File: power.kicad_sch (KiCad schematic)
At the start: 44 parts, among them IC1 MP9943AGQ-Z, IC2 MP9943AGQ-Z, U4 AP2112K-3.3TRG1, U5 AP2112K-1.8TRG1

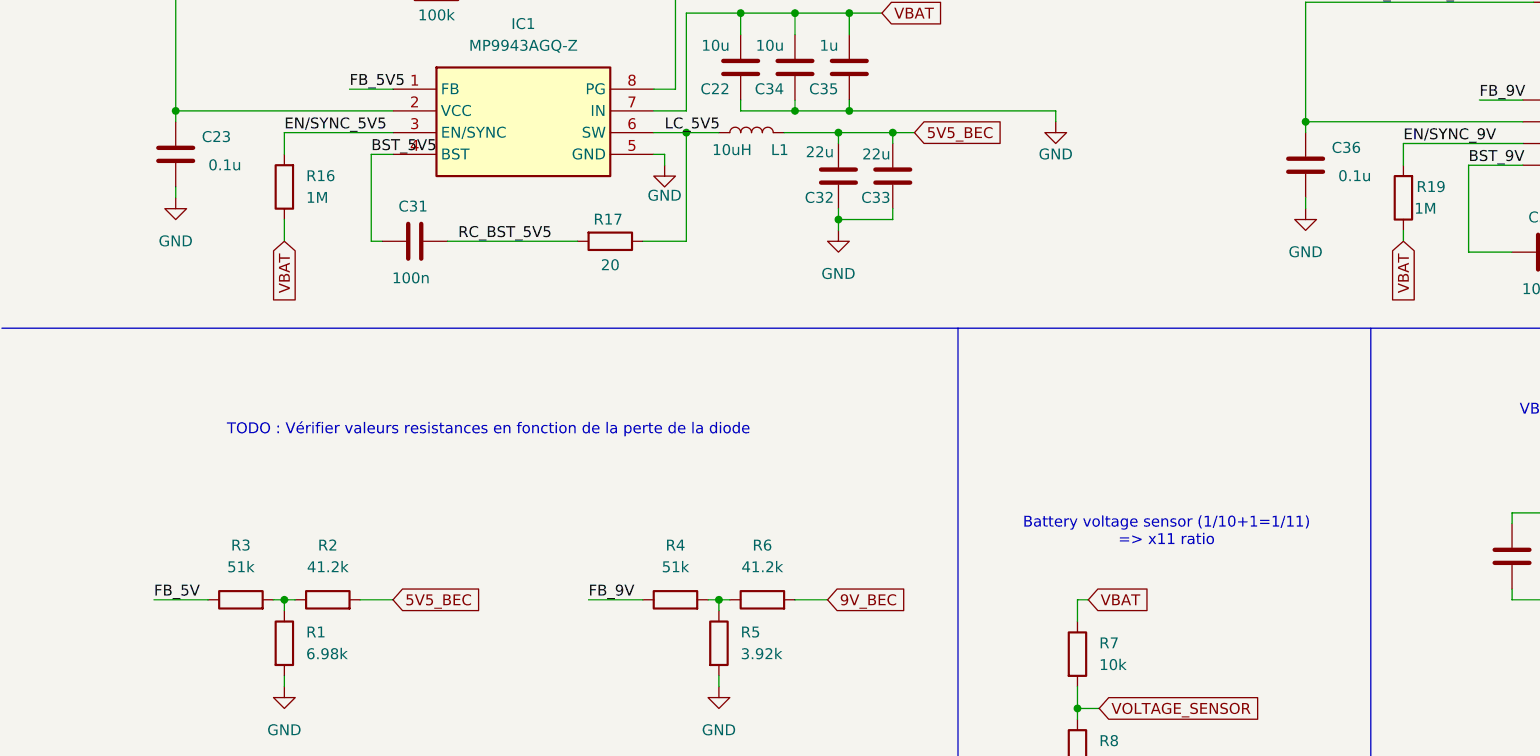
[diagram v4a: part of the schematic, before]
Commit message: - affected footprints for components - started placing components
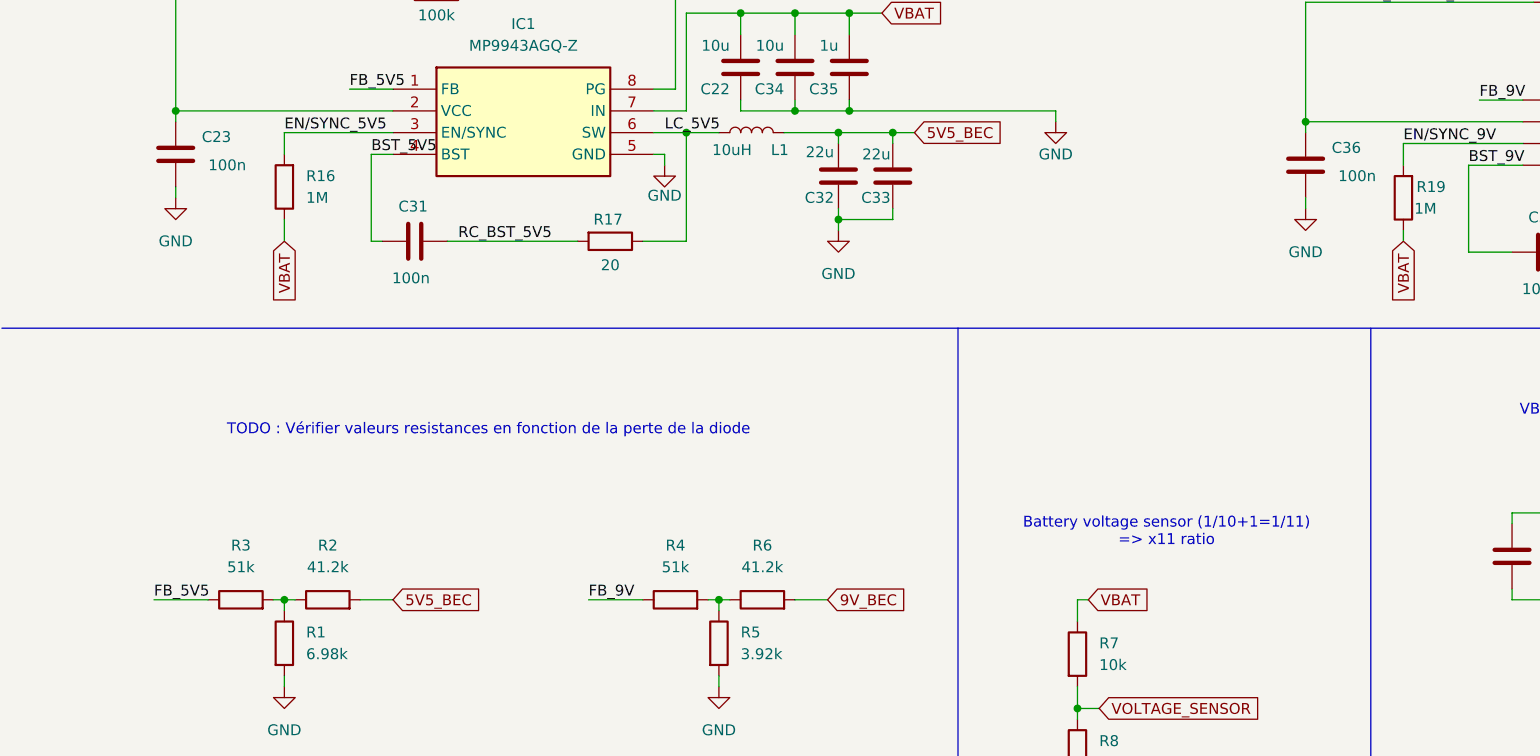
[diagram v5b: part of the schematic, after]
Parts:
- C1, C2, C20, C21, C22, C31, C34, C35, C37, C38, C39, C41: footprint (none) -> Capacitor_SMD:C_0402_1005Metric
- C16, C17, C18, C19, C32, C33, C40, C42: footprint (none) -> Capacitor_SMD:C_0603_1608Metric
- C23, C36: value 0.1u -> 100n; footprint (none) -> Capacitor_SMD:C_0402_1005Metric
- D1, D2: footprint SOD3716X145M -> fcg4_fp:SOD3716X145M
- IC1, IC2: footprint SON65P300X300X100-8M -> fcg4_fp:SON65P300X300X100-8M
- L1, L2: footprint (none) -> Inductor_SMD:L_0603_1608Metric; Manufacturer_Part_Number (none) -> LQM18DH100M70L
- R1, R16, R17, R18, R19, R2, R20, R21, R3, R4, R5, R6, R7, R8: footprint (none) -> Resistor_SMD:R_0402_1005Metric
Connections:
- net FB_5V is gone; now on net FB_5V5: R3.1
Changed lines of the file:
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@@
 		)
 	)
-	(label "FB_5V"
+	(label "FB_5V5"
 		(at 30.48 148.59 0)
 		(effects
@@
 			)
 		)
-		(property "Footprint" ""
+		(property "Footprint" "Capacitor_SMD:C_0402_1005Metric"
 			(at 108.9152 43.18 0)
 			(effects
@@
 			)
 		)
-		(property "Footprint" ""
+		(property "Footprint" "Capacitor_SMD:C_0603_1608Metric"
 			(at 241.6048 96.52 0)
 			(effects
@@
 			)
 		)
-		(property "Footprint" ""
+		(property "Footprint" "Resistor_SMD:R_0402_1005Metric"
 			(at 43.942 153.67 90)
 			(effects
@@
 			)
 		)
-		(property "Footprint" ""
+		(property "Footprint" "Capacitor_SMD:C_0402_1005Metric"
 			(at 104.4448 82.55 0)
 			(effects
@@
 			)
 		)
-		(property "Footprint" ""
+		(property "Footprint" "Capacitor_SMD:C_0603_1608Metric"
 			(at 201.6252 147.32 0)
 			(effects
@@
 			)
 		)
-		(property "Footprint" ""
+		(property "Footprint" "Resistor_SMD:R_0402_1005Metric"
 			(at 94.742 153.67 90)
 			(effects
@@
 			)
 		)
-		(property "Footprint" ""
+		(property "Footprint" "Capacitor_SMD:C_0603_1608Metric"
 			(at 190.1952 147.32 0)
 			(effects
@@
 			)
 		)
-		(property "Footprint" ""
+		(property "Footprint" "Resistor_SMD:R_0402_1005Metric"
 			(at 101.6 150.368 90)
 			(effects
@@
 			)
 		)
-		(property "Footprint" ""
+		(property "Footprint" "Capacitor_SMD:C_0603_1608Metric"
 			(at 247.9548 96.52 0)
 			(effects
@@
 			)
 		)
-		(property "Footprint" ""
+		(property "Footprint" "Capacitor_SMD:C_0603_1608Metric"
 			(at 224.4852 147.32 0)
 			(effects
@@
 			)
 		)
-		(property "Footprint" ""
+		(property "Footprint" "Capacitor_SMD:C_0402_1005Metric"
 			(at 110.7948 82.55 0)
 			(effects
@@
 			)
 		)
-		(property "Footprint" ""
+		(property "Footprint" "Capacitor_SMD:C_0402_1005Metric"
 			(at 98.0948 82.55 0)
 			(effects
@@
 			)
 		)
-		(property "Footprint" ""
+		(property "Footprint" "Resistor_SMD:R_0402_1005Metric"
 			(at 40.64 150.368 90)
 			(effects
@@
 			)
 		)
-		(property "Footprint" ""
+		(property "Footprint" "Capacitor_SMD:C_0603_1608Metric"
 			(at 115.8748 95.25 0)
 			(effects
@@
 			)
 		)
-		(property "Footprint" ""
+		(property "Footprint" "Capacitor_SMD:C_0402_1005Metric"
 			(at 64.77 105.7148 0)
 			(effects
@@
 			)
 		)
-		(property "Footprint" ""
+		(property "Footprint" "Capacitor_SMD:C_0603_1608Metric"
 			(at 213.0552 147.32 0)
 			(effects
@@
 			)
 		)
-		(property "Footprint" ""
+		(property "Footprint" "Capacitor_SMD:C_0402_1005Metric"
 			(at 196.85 106.9848 0)
 			(effects
@@
 			)
 		)
-		(property "Footprint" ""
+		(property "Footprint" "Resistor_SMD:R_0402_1005Metric"
 			(at 47.498 100.33 90)
 			(effects
@@
 			)
 		)
-		(property "Footprint" ""
+		(property "Footprint" "Resistor_SMD:R_0402_1005Metric"
 			(at 50.8 150.368 90)
 			(effects
@@
 			)
 		)
-		(property "Footprint" "SOD3716X145M"
+		(property "Footprint" "fcg4_fp:SOD3716X145M"
 			(at 58.42 -63.17 0)
 			(effects
@@
 			)
 		)
-		(property "Footprint" ""
+		(property "Footprint" "Capacitor_SMD:C_0402_1005Metric"
 			(at 242.8748 83.82 0)
 			(effects
@@
 			)
 		)
-		(property "Footprint" ""
+		(property "Footprint" "Capacitor_SMD:C_0402_1005Metric"
 			(at 230.1748 83.82 0)
 			(effects
@@
 			)
 		)
-		(property "Footprint" "SOD3716X145M"
+		(property "Footprint" "fcg4_fp:SOD3716X145M"
 			(at 41.91 -59.36 0)
 			(effects
@@
 			)
 		)
-		(property "Value" "0.1u"
+		(property "Value" "100n"
 			(at 168.91 99.0599 0)
 			(effects
@@
 			)
 		)
-		(property "Footprint" ""
+		(property "Footprint" "Capacitor_SMD:C_0402_1005Metric"
 			(at 166.0652 101.6 0)
 			(effects
@@
 			)
 		)
-		(property "Footprint" ""
+		(property "Footprint" "Resistor_SMD:R_0402_1005Metric"
 			(at 178.308 101.6 90)
 			(effects
@@
 			)
 		)
-		(property "Footprint" ""
+		(property "Footprint" "Inductor_SMD:L_0603_1608Metric"
 			(at 232.41 95.25 0)
 			(effects
@@
 			)
 		)
+		(property "Manufacturer_Part_Number" "LQM18DH100M70L"
+			(at 232.41 95.25 90)
+			(effects
+				(font
+					(size 1.27 1.27)
+				)
+				(hide yes)
+			)
+		)
 		(pin "1"
 		)
@@
 			)
 		)
-		(property "Footprint" ""
+		(property "Footprint" "Capacitor_SMD:C_0402_1005Metric"
 			(at 196.5452 44.45 0)
 			(effects
@@
 			)
 		)
-		(property "Footprint" ""
+		(property "Footprint" "Resistor_SMD:R_0402_1005Metric"
 			(at 215.9 106.172 90)
 			(effects
@@
 			)
 		)
-		(property "Footprint" ""
+		(property "Footprint" "Resistor_SMD:R_0402_1005Metric"
 			(at 136.652 154.94 90)
 			(effects
@@
 			)
 		)
-		(property "Footprint" ""
+		(property "Footprint" "Capacitor_SMD:C_0402_1005Metric"
 			(at 236.5248 83.82 0)
 			(effects
@@
 			)
 		)
-		(property "Footprint" "SON65P300X300X100-8M"
+		(property "Footprint" "fcg4_fp:SON65P300X300X100-8M"
 			(at 217.17 185.09 0)
 			(effects
@@
 			)
 		)
-		(property "Footprint" ""
+		(property "Footprint" "Resistor_SMD:R_0402_1005Metric"
 			(at 136.652 166.37 90)
 			(effects
@@
 			)
 		)
-		(property "Footprint" ""
+		(property "Footprint" "Resistor_SMD:R_0402_1005Metric"
 			(at 63.5 75.692 90)
 			(effects
@@
 			)
 		)
-		(property "Footprint" ""
+		(property "Footprint" "Inductor_SMD:L_0603_1608Metric"
 			(at 100.33 93.98 0)
 			(effects
@@
 			)
 		)
+		(property "Manufacturer_Part_Number" "LQM18DH100M70L"
+			(at 100.33 93.98 90)
+			(effects
+				(font
+					(size 1.27 1.27)
+				)
+				(hide yes)
+			)
+		)
 		(pin "1"
 		)
@@
 			)
 		)
-		(property "Value" "0.1u"
+		(property "Value" "100n"
 			(at 36.83 97.7899 0)
 			(effects
@@
 			)
 		)
-		(property "Footprint" ""
+		(property "Footprint" "Capacitor_SMD:C_0402_1005Metric"
 			(at 33.9852 100.33 0)
 			(effects
@@
 			)
 		)
-		(property "Footprint" ""
+		(property "Footprint" "Resistor_SMD:R_0402_1005Metric"
 			(at 83.82 104.902 90)
 			(effects
@@
 			)
 		)
-		(property "Footprint" ""
+		(property "Footprint" "Capacitor_SMD:C_0402_1005Metric"
 			(at 73.3552 46.99 0)
 			(effects
@@
 			)
 		)
-		(property "Footprint" ""
+		(property "Footprint" "Resistor_SMD:R_0402_1005Metric"
 			(at 195.58 76.962 90)
 			(effects
@@
 			)
 		)
-		(property "Footprint" ""
+		(property "Footprint" "Capacitor_SMD:C_0603_1608Metric"
 			(at 109.5248 95.25 0)
 			(effects
@@
 			)
 		)
-		(property "Footprint" ""
+		(property "Footprint" "Capacitor_SMD:C_0402_1005Metric"
 			(at 239.7252 44.45 0)
 			(effects
@@
 			)
 		)
-		(property "Footprint" ""
+		(property "Footprint" "Resistor_SMD:R_0402_1005Metric"
 			(at 91.44 150.368 90)
 			(effects
@@
 			)
 		)
-		(property "Footprint" "SON65P300X300X100-8M"
+		(property "Footprint" "fcg4_fp:SON65P300X300X100-8M"
 			(at 85.09 183.82 0)
 			(effects

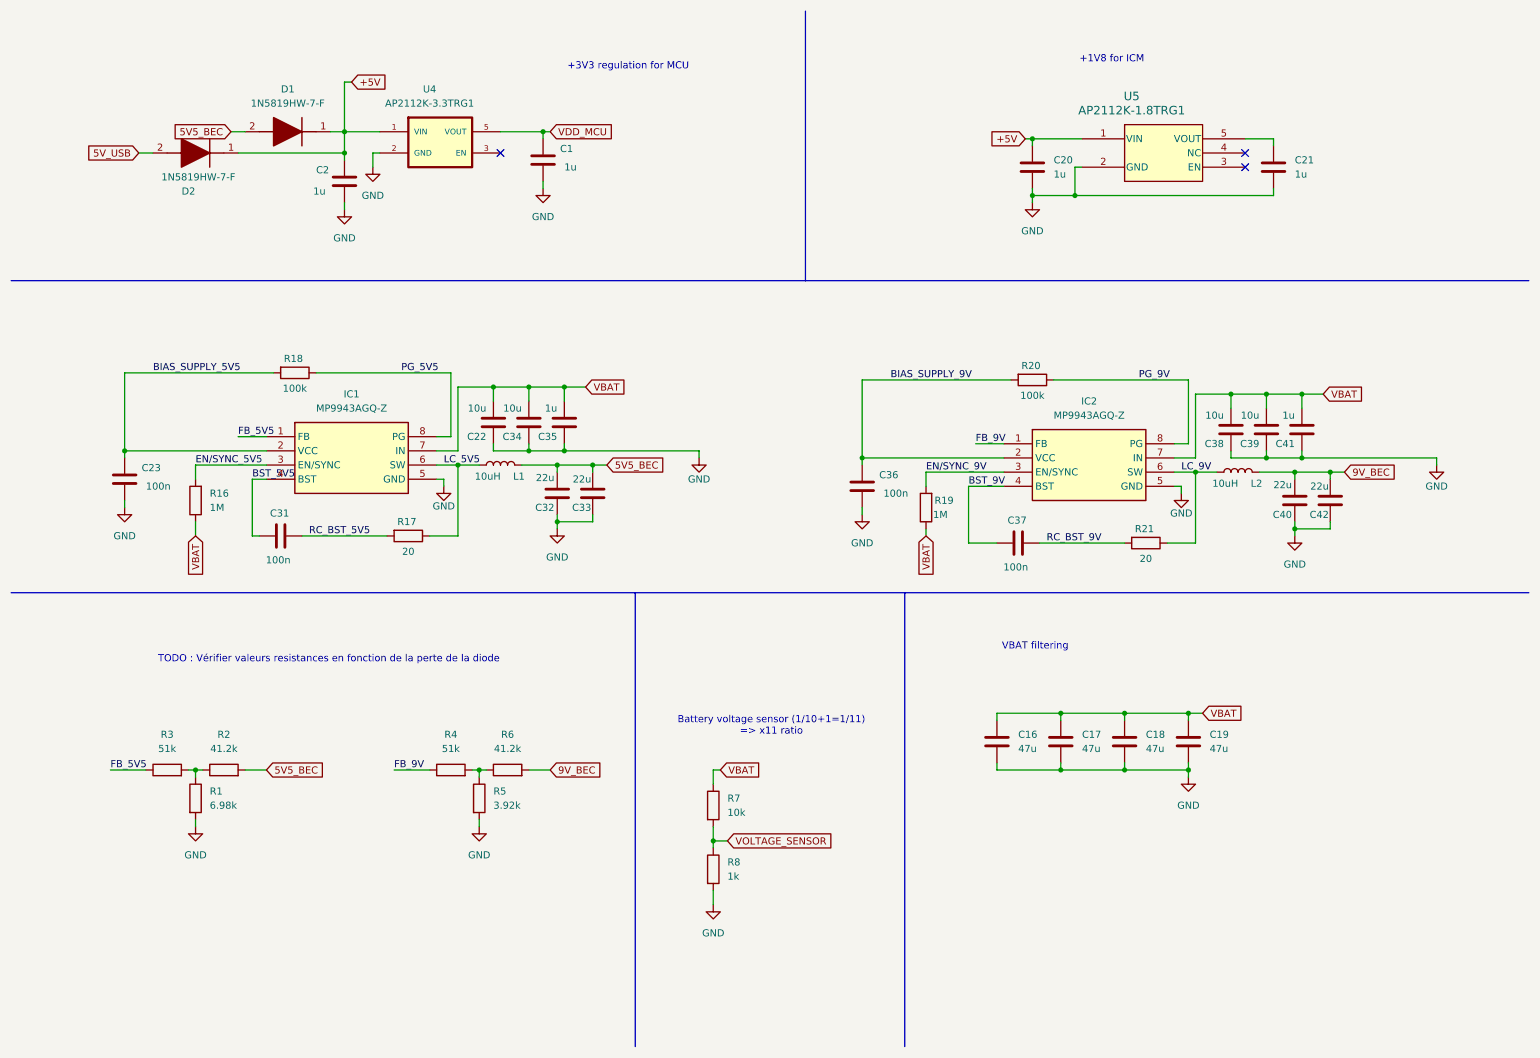
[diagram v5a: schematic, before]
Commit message: Placed every components on one face only
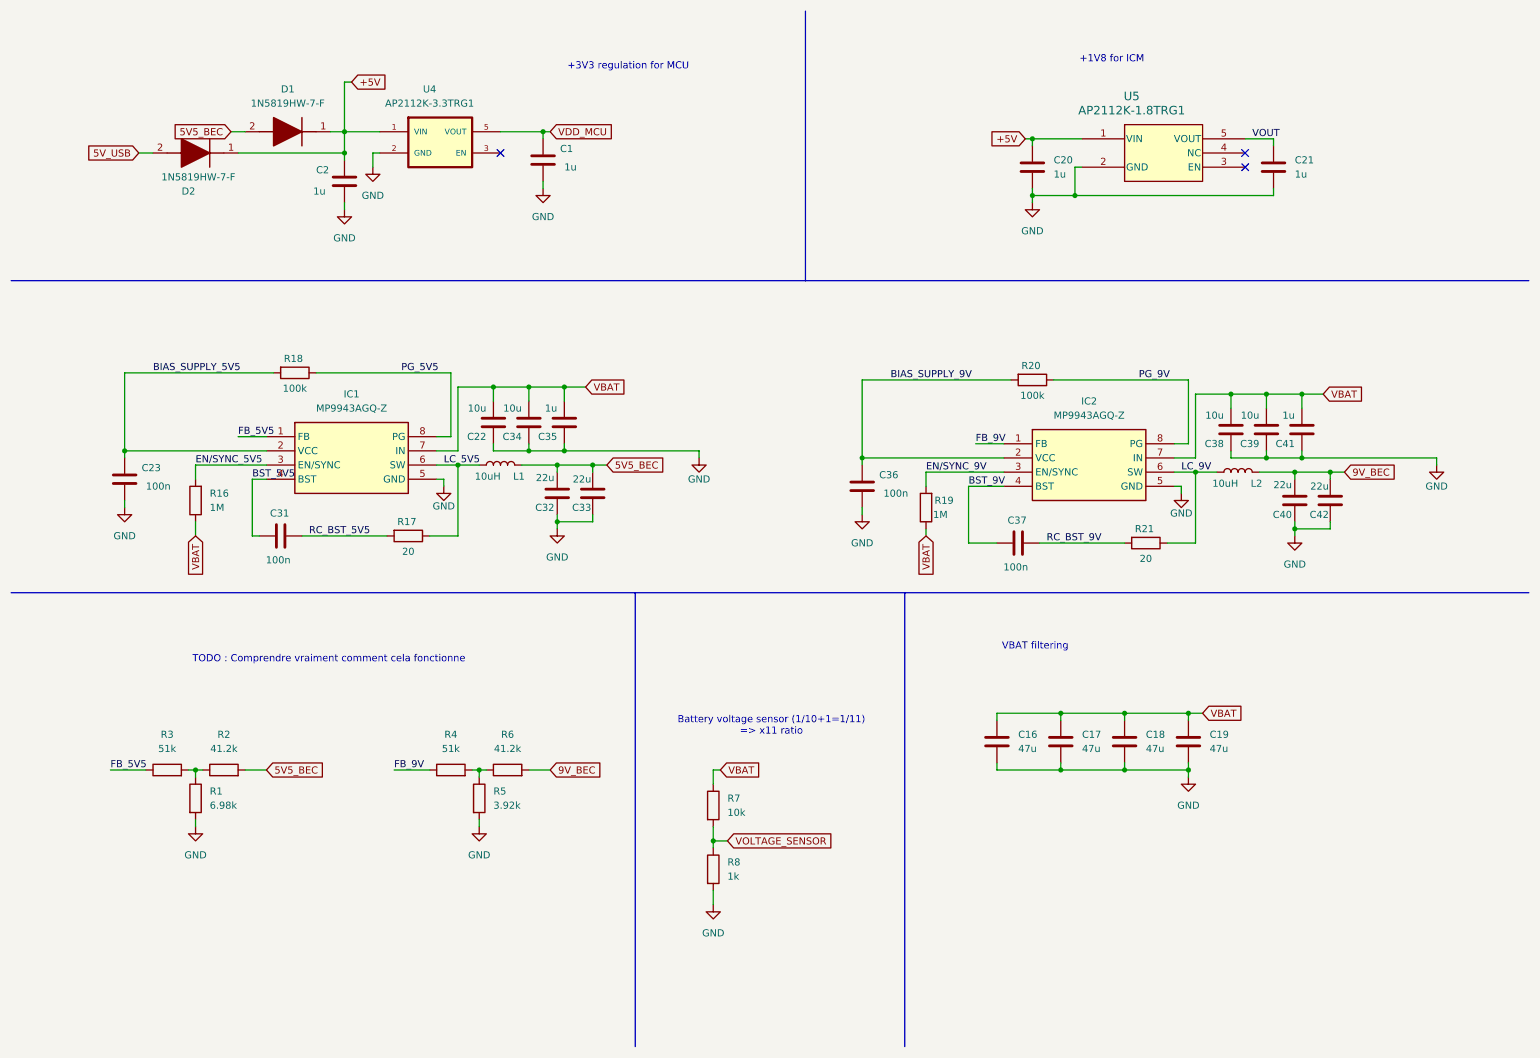
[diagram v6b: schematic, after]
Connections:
- net VOUT: now reaches C21.1, U5.5 (VOUT)
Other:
- note added: "TODO : Comprendre vraiment comment cela fonctionne"
- note removed: "TODO : Vérifier valeurs resistances en fonction de la perte de la diode"
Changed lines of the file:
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@@
 		)
 	)
-	(text "TODO : Vérifier valeurs resistances en fonction de la perte de la diode\n"
+	(text "TODO : Comprendre vraiment comment cela fonctionne"
 		(exclude_from_sim no)
 		(at 69.596 128.778 0)
@@
 		(effects
 			(font
+				(size 1.27 1.27)
+			)
+			(justify left bottom)
+		)
+	)
+	(label "VOUT"
+		(at 234.95 35.56 0)
+		(effects
+			(font
